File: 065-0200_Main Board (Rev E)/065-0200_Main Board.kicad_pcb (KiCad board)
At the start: 6 copper layers, 152.5 x 54.6 mm, 177 parts, among them J1 UJ32-C-H-G-H2-SMT-TR, J2 0022035025, J3 0022035025, J4 custom_3p_2mm, J5 custom_2p_2mm, J6 TC2030-CTX, Q1 CSD25402Q3A, SW1 3-1437565-0, U1 QRE1113GR, U10 LM4875MM/NOPB, U11 TLV313IDBVT, U12 LM393DMR2G, U13 MAX9109EUT+T, U14 TPS63802DLAT, U15 NPM1300-QEAA-R, U16 74LVC1G27GW,12, U2 QRE1113GR, U3 QRE1113GR, U4 BM833, U5 2SMPP03, U6 TLV313IDBVT, U7 INA326, U8 DRV8837DSGR, U9 LM334MX/NOPB, Y1 9HT10-32.768KBZF-T

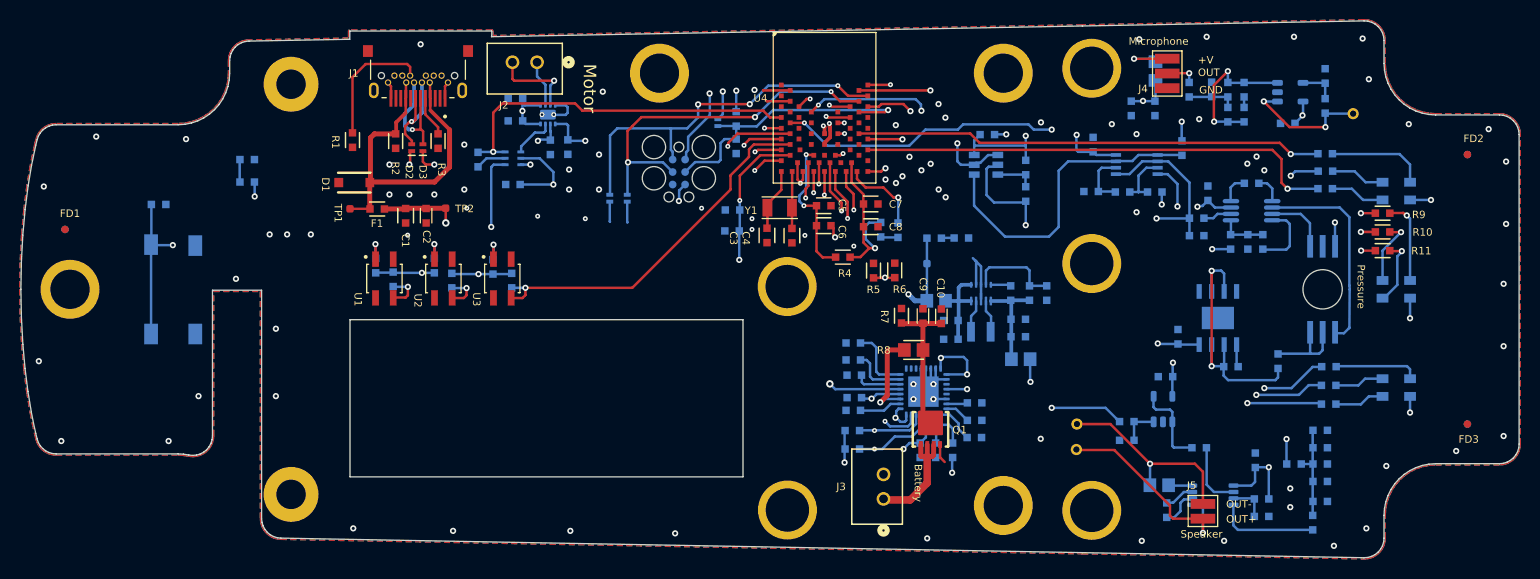
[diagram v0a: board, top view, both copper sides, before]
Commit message: Reset PCB to clean 2-layer layout with fixed enclosure components
- Strip 6-layer Altium PCB down to F.Cu + B.Cu only
- Preserve board outline (149 Edge.Cuts segments)
- Keep 11 mounting holes at original positions
- Lock enclosure-critical components at original positions:
  SW1, U1-U5 (limit sensors, nRF, pressure), J1-J5 (USB-C,
  motor, battery, mic, speaker connectors)
- Preserve BM833 antenna keepout zone
- Fix Altium pin-number artifacts in schematics:
  LED A/K → 1/2, J1 footprint → Amphenol full USB-C,
  Q1 D1/D2/D3/G/S → 5/6/7/8/1, SW1 pins 3/4 → 1/2
- Exclude *.md notes files from git tracking

Co-Authored-By: Claude Sonnet 4.6 <noreply@anthropic.com>
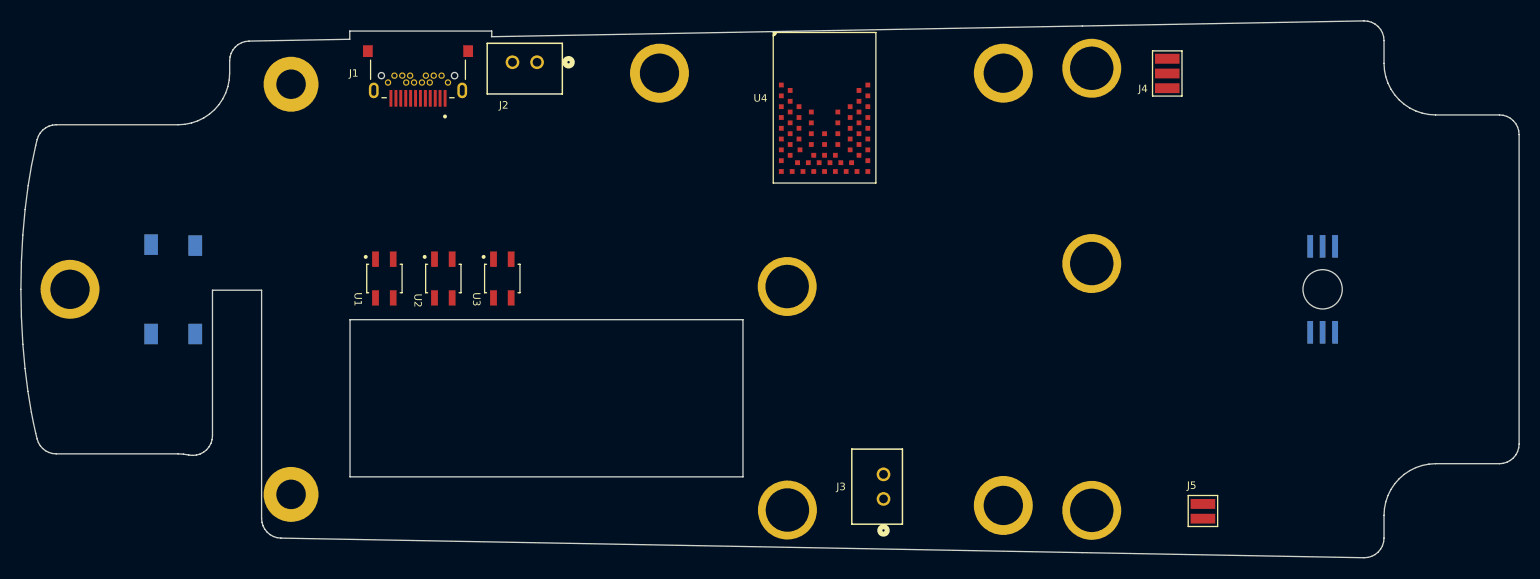
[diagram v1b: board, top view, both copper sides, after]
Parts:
- removed C1, C10, C11, C12, C13, C14, C15, C16, C17, C18, C19, C2, C20, C21, C22, C23, C24, C25, C26, C27, C28, C29, C3, C31, C32, C36, C37, C38, C39, C4, C40, C41, C42, C43, C44, C5, C6, C7, C8, C9: Cap_Ceramic, Discretes:CAP_0603
- removed C30, C33, C34: CL10A226MO7JZNC, Discretes:CAP_0603
- removed C35: C0603C102K5RACTU, Discretes:CAP_0603
- removed D1: ATV02W120B-HF, Discretes:SOD-123_BD
- removed D10, D11, D2, D3, D9: D5V0H1B2LP-7B, Discretes:DFN2_1.01X0.61_0.65P
- removed D12, D7, D8: APT1608ZGCK, Discretes:LED_0603
- removed D4, D5, D6: CLVBA-FKA-CAEDH8BBB7A363, Discretes:LED_PLCC4 - CLVBA
- removed F1: C2Q 2.5, Discretes:RES_0603
- removed FD1, FD2, FD3, FD4, FD5, FD6: DNI, Mechanical:Fiducial_30
- removed J6: TC2030-CTX, Connectors:TC2030_IDC
- removed L1: CIGT252012LMR47MNE, Discretes:L_1008
- removed Q1: CSD25402Q3A, Discretes:Q_8VSON_PCH _NOVIA
- removed R1, R10, R11, R12, R13, R14, R15, R16, R17, R18, R19, R2, R20, R21, R22, R23, R24, R25, R26, R27, R29, R3, R30, R31, R32, R33, R35, R37, R38, R39, R4, R40, R41, R43, R44, R45, R46, R47, R48, R49, R5, R51, R52, R53, R54, R55, R56, R57, R58, R59, R6, R60, R61, R62, R63, R64, R65, R66, R67, R68, R69, R7, R70, R71, R9: Resistor, Discretes:RES_0603
- removed R28: ERJ-3EKF6810V, Discretes:RES_0603
- removed R34, R36, R42, R50, R8: Resistor, Discretes:RES_0805
- removed TP1, TP2, TP7: TP SMT Round 30mil, Connectors:TP_SMT_0.030
- removed TP3, TP4, TP5: TP TH Round 45 mil sqr, 25mil hole, Connectors:TP_TH_45-25
- removed U10: LM4875MM/NOPB, IC packages:MSOP-8_MPS
- removed U11, U6: TLV313IDBVT, IC packages:SOT-23-5
- removed U12: LM393DMR2G, IC packages:MICRO8 3.3X3.3.1
- removed U13: MAX9109EUT+T, IC packages:SOT23-6
- removed U14: TPS63802DLAT, IC packages:TI-VSON-HR-10
- removed U15: NPM1300-QEAA-R, IC packages:QFN-32_5X5_EXP
- removed U16: 74LVC1G27GW,12, IC packages:SOT_363
- removed U7: INA326, IC packages:TSSOP-8_3x3
- removed U8: DRV8837DSGR, IC packages:WSON_8_2X2
- removed U9: LM334MX/NOPB, IC packages:8-SOIC
- removed Y1: 9HT10-32.768KBZF-T, Discretes:Y_2PIN_3.2mmX1.5mm
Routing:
- net +3V3: track 133.9 -> 0.00 mm, vias 27 -> 0
- net NetC44_1: track 109.6 -> 0.00 mm, vias 3 -> 0
- net GND: track 96.7 -> 0.00 mm, vias 74 -> 0
- net VBUS: track 94.1 -> 0.00 mm, vias 4 -> 0
- net PWM_VOL: track 85.9 -> 0.00 mm, vias 4 -> 0
- net BLE_R: track 82.5 -> 0.00 mm, vias 5 -> 0
- net BLE_B: track 79.0 -> 0.00 mm, vias 4 -> 0
- net ENV_OUT: track 78.4 -> 0.00 mm, vias 5 -> 0
- net BLE_G: track 76.1 -> 0.00 mm, vias 4 -> 0
- net MEAS_B: track 68.8 -> 0.00 mm, vias 4 -> 0
- net MEAS_G: track 68.0 -> 0.00 mm, vias 4 -> 0
- net 226HZ: track 64.6 -> 0.00 mm, vias 3 -> 0
- net MEAS_R: track 62.0 -> 0.00 mm, vias 4 -> 0
- net USB_D_P: track 58.6 -> 0.00 mm, vias 2 -> 0
- net Back_Limit: track 56.6 -> 0.00 mm, vias 4 -> 0
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- removed copper zone on In4.Cu, net +3V3
- removed copper zone on B.Cu, net GND
- removed copper zone on F.Cu, net GND
- removed copper zone on In1.Cu, net GND
- removed copper zone on In2.Cu, net GND
- removed copper zone on In3.Cu, net GND
- removed copper zone on In4.Cu, net VSys
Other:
- copper layers 6 -> 2
- rule pad_to_mask_clearance: 0.0508 -> 0
- board text removed: "${PROJECT_PART_NUMBER_PCB}"
- board text removed: "+3.3V"
- board text removed: "+V"
- board text removed: "+Vsys"
- board text removed: "BLE"
- board text removed: "Batt"
- board text removed: "Battery"
- board text removed: "ENV OUT"
- board text removed: "GND"
- board text removed: "Meas"
- board text removed: "Microphone"
- board text removed: "Motor"
- board text removed: "OUT"
- board text removed: "OUT+"
- board text removed: "OUT-"
- board text removed: "Pressure"
- board text removed: "Rev: .Project_Revision_PCB"
- board text removed: "Speaker"

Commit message: Add OLED connector, annotate schematics, place all components on B.Cu
- Added J7 (GME12864-13 OLED) 4-pin I2C connector on Page 3 Micro,
  wired to SDA/SCL nets shared with the nRF module
- Auto-annotated power symbols across all schematic pages (#PWR? → numbered)
- Ran Update PCB from Schematic; all components placed on B.Cu
  ready for manual placement and routing

Co-Authored-By: Claude Sonnet 4.6 <noreply@anthropic.com>
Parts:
- added C1: Cap_Ceramic, Capacitor_SMD:C_0603_1608Metric, B.Cu at (76.3, 138.3)
- added C10: Cap_Ceramic, Capacitor_SMD:C_0603_1608Metric, B.Cu at (76.3, 145.8)
- added C11: Cap_Ceramic, Capacitor_SMD:C_0603_1608Metric, B.Cu at (98.2, 178.5)
- added C12: Cap_Ceramic, Capacitor_SMD:C_0603_1608Metric, B.Cu at (98.2, 181.1)
- added C13: Cap_Ceramic, Capacitor_SMD:C_0603_1608Metric, B.Cu at (98.2, 183.6)
- added C14: Cap_Ceramic, Capacitor_SMD:C_0603_1608Metric, B.Cu at (54.3, 138.3)
- added C15: Cap_Ceramic, Capacitor_SMD:C_0603_1608Metric, B.Cu at (54.3, 140.8)
- added C16: Cap_Ceramic, Capacitor_SMD:C_0603_1608Metric, B.Cu at (98.2, 186.1)
- added C17: Cap_Ceramic, Capacitor_SMD:C_0603_1608Metric, B.Cu at (54.3, 143.3)
- added C18: Cap_Ceramic, Capacitor_SMD:C_0603_1608Metric, B.Cu at (54.3, 145.8)
- added C19: Cap_Ceramic, Capacitor_SMD:C_0603_1608Metric, B.Cu at (54.3, 148.3)
- added C2: Cap_Ceramic, Capacitor_SMD:C_0603_1608Metric, B.Cu at (76.3, 140.8)
- added C20: Cap_Ceramic, Capacitor_SMD:C_0603_1608Metric, B.Cu at (54.3, 150.8)
- added C21: Cap_Ceramic, Capacitor_SMD:C_0603_1608Metric, B.Cu at (98.2, 188.6)
- added C22: Cap_Ceramic, Capacitor_SMD:C_0603_1608Metric, B.Cu at (54.3, 153.3)
- added C23: Cap_Ceramic, Capacitor_SMD:C_0603_1608Metric, B.Cu at (54.3, 155.8)
- added C24: Cap_Ceramic, Capacitor_SMD:C_0603_1608Metric, B.Cu at (98.2, 191.1)
- added C25: Cap_Ceramic, Capacitor_SMD:C_0603_1608Metric, B.Cu at (94.2, 178.5)
- added C26: Cap_Ceramic, Capacitor_SMD:C_0603_1608Metric, B.Cu at (50.3, 138.3)
- added C27: Cap_Ceramic, Capacitor_SMD:C_0603_1608Metric, B.Cu at (50.3, 140.8)
- added C28: Cap_Ceramic, Capacitor_SMD:C_0603_1608Metric, B.Cu at (94.2, 181.1)
- added C29: Cap_Ceramic, Capacitor_SMD:C_0603_1608Metric, B.Cu at (50.3, 143.3)
- added C3: Cap_Ceramic, Capacitor_SMD:C_0603_1608Metric, B.Cu at (54.3, 169.3)
- added C30: CL10A226MO7JZNC, Capacitor_SMD:C_0603_1608Metric, B.Cu at (76.3, 148.3)
- added C31: Cap_Ceramic, Capacitor_SMD:C_0603_1608Metric, B.Cu at (76.3, 150.8)
- added C32: Cap_Ceramic, Capacitor_SMD:C_0603_1608Metric, B.Cu at (50.3, 145.8)
- added C33: CL10A226MO7JZNC, Capacitor_SMD:C_0603_1608Metric, B.Cu at (72.3, 138.3)
- added C34: CL10A226MO7JZNC, Capacitor_SMD:C_0603_1608Metric, B.Cu at (72.3, 140.8)
- added C35: C0603C102K5RACTU, Capacitor_SMD:C_0603_1608Metric, B.Cu at (72.3, 143.3)
- added C36: Cap_Ceramic, Capacitor_SMD:C_0603_1608Metric, B.Cu at (72.3, 145.8)
- added C37: Cap_Ceramic, Capacitor_SMD:C_0603_1608Metric, B.Cu at (72.3, 148.3)
- added C38: Cap_Ceramic, Capacitor_SMD:C_0603_1608Metric, B.Cu at (54.3, 184.3)
- added C39: Cap_Ceramic, Capacitor_SMD:C_0603_1608Metric, B.Cu at (50.3, 169.3)
- added C4: Cap_Ceramic, Capacitor_SMD:C_0603_1608Metric, B.Cu at (54.3, 171.8)
- added C40: Cap_Ceramic, Capacitor_SMD:C_0603_1608Metric, B.Cu at (50.3, 171.8)
- added C41: Cap_Ceramic, Capacitor_SMD:C_0603_1608Metric, B.Cu at (79.2, 178.5)
- added C42: Cap_Ceramic, Capacitor_SMD:C_0603_1608Metric, B.Cu at (79.2, 181.1)
- added C43: Cap_Ceramic, Capacitor_SMD:C_0603_1608Metric, B.Cu at (79.2, 183.6)
- added C44: Cap_Ceramic, Capacitor_SMD:C_0603_1608Metric, B.Cu at (72.3, 150.8)
- added C5: Cap_Ceramic, Capacitor_SMD:C_0603_1608Metric, B.Cu at (54.3, 174.3)
- added C6: Cap_Ceramic, Capacitor_SMD:C_0603_1608Metric, B.Cu at (54.3, 176.8)
- added C7: Cap_Ceramic, Capacitor_SMD:C_0603_1608Metric, B.Cu at (54.3, 179.3)
- added C8: Cap_Ceramic, Capacitor_SMD:C_0603_1608Metric, B.Cu at (54.3, 181.8)
- added C9: Cap_Ceramic, Capacitor_SMD:C_0603_1608Metric, B.Cu at (76.3, 143.3)
- added D1: ATV02W120B-HF, Diode_SMD:D_SOD-123, B.Cu at (89.8, 173.6)
- added D10: D5V0H1B2LP-7B, Package_TO_SOT_SMD:SOT-883, B.Cu at (46.9, 189.1)
- added D11: D5V0H1B2LP-7B, Package_TO_SOT_SMD:SOT-883, B.Cu at (46.9, 191.4)
- added D12: APT1608ZGCK, LED_SMD:LED_0603_1608Metric, B.Cu at (64.5, 163.3)
- added D2: D5V0H1B2LP-7B, Package_TO_SOT_SMD:SOT-883, B.Cu at (61.1, 160.5)
- added D3: D5V0H1B2LP-7B, Package_TO_SOT_SMD:SOT-883, B.Cu at (61.1, 162.9)
- added D4: CLVBA-FKA-CAEDH8BBB7A363, LED_SMD:LED_Cree-PLCC4_3.2x2.8mm_CCW, B.Cu at (37.7, 170.2)
- added D4: CLVBA-FKA-CAEDH8BBB7A363, LED_SMD:LED_Cree-PLCC4_3.2x2.8mm_CCW, B.Cu at (212.3, 95.0)
- added D5: CLVBA-FKA-CAEDH8BBB7A363, LED_SMD:LED_Cree-PLCC4_3.2x2.8mm_CCW, B.Cu at (212.3, 105.0)
- added D5: CLVBA-FKA-CAEDH8BBB7A363, LED_SMD:LED_Cree-PLCC4_3.2x2.8mm_CCW, B.Cu at (37.7, 174.5)
- added D6: CLVBA-FKA-CAEDH8BBB7A363, LED_SMD:LED_Cree-PLCC4_3.2x2.8mm_CCW, B.Cu at (212.3, 115.0)
- added D6: CLVBA-FKA-CAEDH8BBB7A363, LED_SMD:LED_Cree-PLCC4_3.2x2.8mm_CCW, B.Cu at (37.7, 178.9)
- added D7: APT1608ZGCK, LED_SMD:LED_0603_1608Metric, B.Cu at (64.5, 160.7)
- added D8: APT1608ZGCK, LED_SMD:LED_0603_1608Metric, B.Cu at (43.6, 190.2)
- added D9: D5V0H1B2LP-7B, Package_TO_SOT_SMD:SOT-883, B.Cu at (46.9, 186.7)
- added F1: C2Q 2.5, Resistor_SMD:R_0603_1608Metric, B.Cu at (68.3, 138.3)
- added FD1: DNI, Fiducial:Fiducial_1mm_Mask2mm, B.Cu at (76.6, 166.5)
- added FD2: DNI, Fiducial:Fiducial_1mm_Mask2mm, B.Cu at (76.6, 170.0)
- added FD3: DNI, Fiducial:Fiducial_1mm_Mask2mm, B.Cu at (73.0, 166.5)
- added FD4: DNI, Fiducial:Fiducial_1mm_Mask2mm, B.Cu at (73.0, 170.0)
- added FD5: DNI, Fiducial:Fiducial_1mm_Mask2mm, B.Cu at (69.5, 166.5)
- added FD6: DNI, Fiducial:Fiducial_1mm_Mask2mm, B.Cu at (69.5, 170.0)
- added J1: UJ32-C-H-G-H2-SMT-TR, Connector_USB:USB_C_Receptacle_Amphenol_12401548E4-2A, B.Cu at (72.4, 158.5)
- added J2: 0022035025, Connector_PinHeader_2.54mm:PinHeader_1x02_P2.54mm_Vertical, B.Cu at (70.9, 192.0)
- added J3: 0022035025, Connector_PinHeader_2.54mm:PinHeader_1x02_P2.54mm_Vertical, B.Cu at (90.4, 167.1)
- added J4: custom_3p_2mm, Connector_PinHeader_2.00mm:PinHeader_1x03_P2.00mm_Vertical, B.Cu at (54.3, 159.1)
- added J5: custom_2p_2mm, Connector_PinHeader_2.00mm:PinHeader_1x02_P2.00mm_Vertical, B.Cu at (86.1, 179.3)
- added J6: TC2030-CTX, Connector:Tag-Connect_TC2030-IDC-NL_2x03_P1.27mm_Vertical, B.Cu at (52.3, 188.1)
- added J7: Conn_01x04_Pin, Connector_PinHeader_2.54mm:PinHeader_1x04_P2.54mm_Vertical, B.Cu at (38.0, 183.3)
- added L1: CIGT252012LMR47MNE, Inductor_SMD:L_1008_2520Metric, B.Cu at (65.2, 173.1)
- added Q1: CSD25402Q3A, Package_SON:WSON-8-1EP_2x2mm_P0.5mm_EP0.9x1.6mm, B.Cu at (60.5, 173.2)
- added R1: Resistor, Resistor_SMD:R_0603_1608Metric, B.Cu at (68.3, 140.8)
- added R10: Resistor, Resistor_SMD:R_0603_1608Metric, B.Cu at (50.3, 184.3)
- added R11: Resistor, Resistor_SMD:R_0603_1608Metric, B.Cu at (46.3, 169.3)
- added R12: Resistor, Resistor_SMD:R_0603_1608Metric, B.Cu at (46.3, 171.8)
- added R13: Resistor, Resistor_SMD:R_0603_1608Metric, B.Cu at (46.3, 174.3)
- added R14: Resistor, Resistor_SMD:R_0603_1608Metric, B.Cu at (46.3, 176.8)
- added R15: Resistor, Resistor_SMD:R_0603_1608Metric, B.Cu at (46.3, 179.3)
- added R16: Resistor, Resistor_SMD:R_0603_1608Metric, B.Cu at (46.3, 181.8)
- added R17: Resistor, Resistor_SMD:R_0603_1608Metric, B.Cu at (46.3, 184.3)
- added R18: Resistor, Resistor_SMD:R_0603_1608Metric, B.Cu at (50.3, 148.3)
- added R19: Resistor, Resistor_SMD:R_0603_1608Metric, B.Cu at (50.3, 150.8)
- added R2: Resistor, Resistor_SMD:R_0603_1608Metric, B.Cu at (68.3, 143.3)
- added R20: Resistor, Resistor_SMD:R_0603_1608Metric, B.Cu at (94.2, 183.6)
- added R21: Resistor, Resistor_SMD:R_0603_1608Metric, B.Cu at (94.2, 186.1)
- added R22: Resistor, Resistor_SMD:R_0603_1608Metric, B.Cu at (50.3, 153.3)
- added R23: Resistor, Resistor_SMD:R_0603_1608Metric, B.Cu at (94.2, 188.6)
- added R24: Resistor, Resistor_SMD:R_0603_1608Metric, B.Cu at (94.2, 191.1)
- added R25: Resistor, Resistor_SMD:R_0603_1608Metric, B.Cu at (50.3, 155.8)
- added R26: Resistor, Resistor_SMD:R_0603_1608Metric, B.Cu at (46.3, 138.3)
- added R27: Resistor, Resistor_SMD:R_0603_1608Metric, B.Cu at (46.3, 140.8)
- added R28: ERJ-3EKF6810V, Resistor_SMD:R_0603_1608Metric, B.Cu at (46.3, 143.3)
- added R29: Resistor, Resistor_SMD:R_0603_1608Metric, B.Cu at (46.3, 145.8)
- added R3: Resistor, Resistor_SMD:R_0603_1608Metric, B.Cu at (68.3, 145.8)
- added R30: Resistor, Resistor_SMD:R_0603_1608Metric, B.Cu at (46.3, 148.3)
- added R31: Resistor, Resistor_SMD:R_0603_1608Metric, B.Cu at (46.3, 150.8)
- added R32: Resistor, Resistor_SMD:R_0603_1608Metric, B.Cu at (46.3, 153.3)
- added R33: Resistor, Resistor_SMD:R_0603_1608Metric, B.Cu at (46.3, 155.8)
- added R34: Resistor, Resistor_SMD:R_0805_2012Metric, B.Cu at (85.4, 193.8)
- added R35: Resistor, Resistor_SMD:R_0603_1608Metric, B.Cu at (42.3, 138.3)
- added R36: Resistor, Resistor_SMD:R_0805_2012Metric, B.Cu at (50.0, 163.2)
- added R37: Resistor, Resistor_SMD:R_0603_1608Metric, B.Cu at (90.2, 178.5)
- added R38: Resistor, Resistor_SMD:R_0603_1608Metric, B.Cu at (42.3, 140.8)
- added R39: Resistor, Resistor_SMD:R_0603_1608Metric, B.Cu at (42.3, 143.3)
- added R4: Resistor, Resistor_SMD:R_0603_1608Metric, B.Cu at (50.3, 174.3)
- added R40: Resistor, Resistor_SMD:R_0603_1608Metric, B.Cu at (68.3, 150.8)
- added R41: Resistor, Resistor_SMD:R_0603_1608Metric, B.Cu at (64.3, 138.3)
- added R42: Resistor, Resistor_SMD:R_0805_2012Metric, B.Cu at (98.0, 169.2)
- added R43: Resistor, Resistor_SMD:R_0603_1608Metric, B.Cu at (42.3, 145.8)
- added R44: Resistor, Resistor_SMD:R_0603_1608Metric, B.Cu at (42.3, 148.3)
- added R45: Resistor, Resistor_SMD:R_0603_1608Metric, B.Cu at (64.3, 140.8)
- added R46: Resistor, Resistor_SMD:R_0603_1608Metric, B.Cu at (64.3, 143.3)
- added R47: Resistor, Resistor_SMD:R_0603_1608Metric, B.Cu at (64.3, 145.8)
- added R48: Resistor, Resistor_SMD:R_0603_1608Metric, B.Cu at (64.3, 148.3)
- added R49: Resistor, Resistor_SMD:R_0603_1608Metric, B.Cu at (64.3, 150.8)
- added R5: Resistor, Resistor_SMD:R_0603_1608Metric, B.Cu at (50.3, 176.8)
- added R50: Resistor, Resistor_SMD:R_0805_2012Metric, B.Cu at (98.0, 172.2)
- added R51: Resistor, Resistor_SMD:R_0603_1608Metric, B.Cu at (60.3, 138.3)
- added R52: Resistor, Resistor_SMD:R_0603_1608Metric, B.Cu at (60.3, 140.8)
- added R53: Resistor, Resistor_SMD:R_0603_1608Metric, B.Cu at (42.3, 169.3)
- added R54: Resistor, Resistor_SMD:R_0603_1608Metric, B.Cu at (60.3, 143.3)
- added R55: Resistor, Resistor_SMD:R_0603_1608Metric, B.Cu at (60.3, 145.8)
- added R56: Resistor, Resistor_SMD:R_0603_1608Metric, B.Cu at (60.3, 148.3)
- added R57: Resistor, Resistor_SMD:R_0603_1608Metric, B.Cu at (42.3, 171.8)
- added R58: Resistor, Resistor_SMD:R_0603_1608Metric, B.Cu at (42.3, 174.3)
- added R59: Resistor, Resistor_SMD:R_0603_1608Metric, B.Cu at (42.3, 176.8)
- added R6: Resistor, Resistor_SMD:R_0603_1608Metric, B.Cu at (50.3, 179.3)
- added R60: Resistor, Resistor_SMD:R_0603_1608Metric, B.Cu at (79.2, 186.1)
- added R61: Resistor, Resistor_SMD:R_0603_1608Metric, B.Cu at (79.2, 188.6)
- added R62: Resistor, Resistor_SMD:R_0603_1608Metric, B.Cu at (79.2, 191.1)
- added R63: Resistor, Resistor_SMD:R_0603_1608Metric, B.Cu at (75.2, 178.5)
- added R64: Resistor, Resistor_SMD:R_0603_1608Metric, B.Cu at (42.3, 179.3)
- added R65: Resistor, Resistor_SMD:R_0603_1608Metric, B.Cu at (75.2, 181.1)
- added R66: Resistor, Resistor_SMD:R_0603_1608Metric, B.Cu at (75.2, 183.6)
- added R67: Resistor, Resistor_SMD:R_0603_1608Metric, B.Cu at (75.2, 186.1)
- added R68: Resistor, Resistor_SMD:R_0603_1608Metric, B.Cu at (75.2, 188.6)
- added R69: Resistor, Resistor_SMD:R_0603_1608Metric, B.Cu at (60.3, 150.8)
- added R7: Resistor, Resistor_SMD:R_0603_1608Metric, B.Cu at (68.3, 148.3)
- added R70: Resistor, Resistor_SMD:R_0603_1608Metric, B.Cu at (90.2, 181.1)
- added R71: Resistor, Resistor_SMD:R_0603_1608Metric, B.Cu at (90.2, 183.6)
- added R8: Resistor, Resistor_SMD:R_0805_2012Metric, B.Cu at (98.0, 166.3)
- added R9: Resistor, Resistor_SMD:R_0603_1608Metric, B.Cu at (50.3, 181.8)
- added SW1: 3-1437565-0, Button_Switch_SMD:Panasonic_EVQPUL_EVQPUC, B.Cu at (63.3, 168.5)
- added TP1: TP SMT Round 30mil, TestPoint:TestPoint_Pad_D1.0mm, B.Cu at (94.3, 166.3)
- added TP2: TP SMT Round 30mil, TestPoint:TestPoint_Pad_D1.0mm, B.Cu at (94.3, 169.4)
- added TP3: TP TH Round 45 mil sqr, 25mil hole, TestPoint:TestPoint_THTPad_D1.5mm_Drill0.7mm, B.Cu at (43.5, 158.9)
- added TP4: TP TH Round 45 mil sqr, 25mil hole, TestPoint:TestPoint_THTPad_D1.5mm_Drill0.7mm, B.Cu at (86.4, 185.1)
- added TP5: TP TH Round 45 mil sqr, 25mil hole, TestPoint:TestPoint_THTPad_D1.5mm_Drill0.7mm, B.Cu at (86.4, 188.7)
- added TP7: TP SMT Round 30mil, TestPoint:TestPoint_Pad_D1.0mm, B.Cu at (94.3, 172.4)
- added U1: QRE1113GR, Package_SO:SOIC-4_4.55x2.6mm_P1.27mm, B.Cu at (68.4, 179.4)
- added U10: LM4875MM/NOPB, Package_SO:MSOP-8_3x3mm_P0.65mm, B.Cu at (96.5, 194.7)
- added U11: TLV313IDBVT, Package_TO_SOT_SMD:SOT-23-5, B.Cu at (90.2, 194.8)
- added U12: LM393DMR2G, Package_SO:SOIC-8_3.9x4.9mm_P1.27mm, B.Cu at (36.0, 153.5)
- added U13: MAX9109EUT+T, Package_TO_SOT_SMD:SOT-23-6, B.Cu at (37.7, 163.8)
- added U14: TPS63802DLAT, Package_SON:VSON-10-1EP_3x3mm_P0.5mm_EP1.65x2.4mm, B.Cu at (83.6, 171.5)
- added U15: NPM1300-QEAA-R, Package_DFN_QFN:QFN-32-1EP_5x5mm_P0.5mm_EP3.1x3.1mm, B.Cu at (62.5, 155.7)
- added U16: 74LVC1G27GW,12, Package_TO_SOT_SMD:SOT-363_SC-70-6, B.Cu at (79.2, 194.2)
- added U2: QRE1113GR, Package_SO:SOIC-4_4.55x2.6mm_P1.27mm, B.Cu at (68.4, 183.5)
- added U3: QRE1113GR, Package_SO:SOIC-4_4.55x2.6mm_P1.27mm, B.Cu at (68.4, 187.7)
- added U5: 2SMPP03, Package_SO:SOIC-8_3.9x4.9mm_P1.27mm, B.Cu at (35.7, 140.4)
- added U6: TLV313IDBVT, Package_TO_SOT_SMD:SOT-23-5, B.Cu at (37.7, 159.2)
- added U7: INA326, Package_SO:TSSOP-8_3x3mm_P0.65mm, B.Cu at (48.8, 159.4)
- added U8: DRV8837DSGR, Package_SON:WSON-8-1EP_2x2mm_P0.5mm_EP0.9x1.6mm, B.Cu at (66.4, 191.7)
- added U9: LM334MX/NOPB, Package_SO:SOIC-8_3.9x4.9mm_P1.27mm, B.Cu at (36.0, 146.9)
- added Y1: 9HT10-32.768KBZF-T, Crystal:Crystal_SMD_3215-2Pin_3.2x1.5mm, B.Cu at (43.1, 187.2)
